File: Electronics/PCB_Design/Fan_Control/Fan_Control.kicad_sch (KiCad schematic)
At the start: 3 parts, among them J2 Conn_01x03, Q1 Q_NMOS_GSD, U1 SeeeduinoXIAO

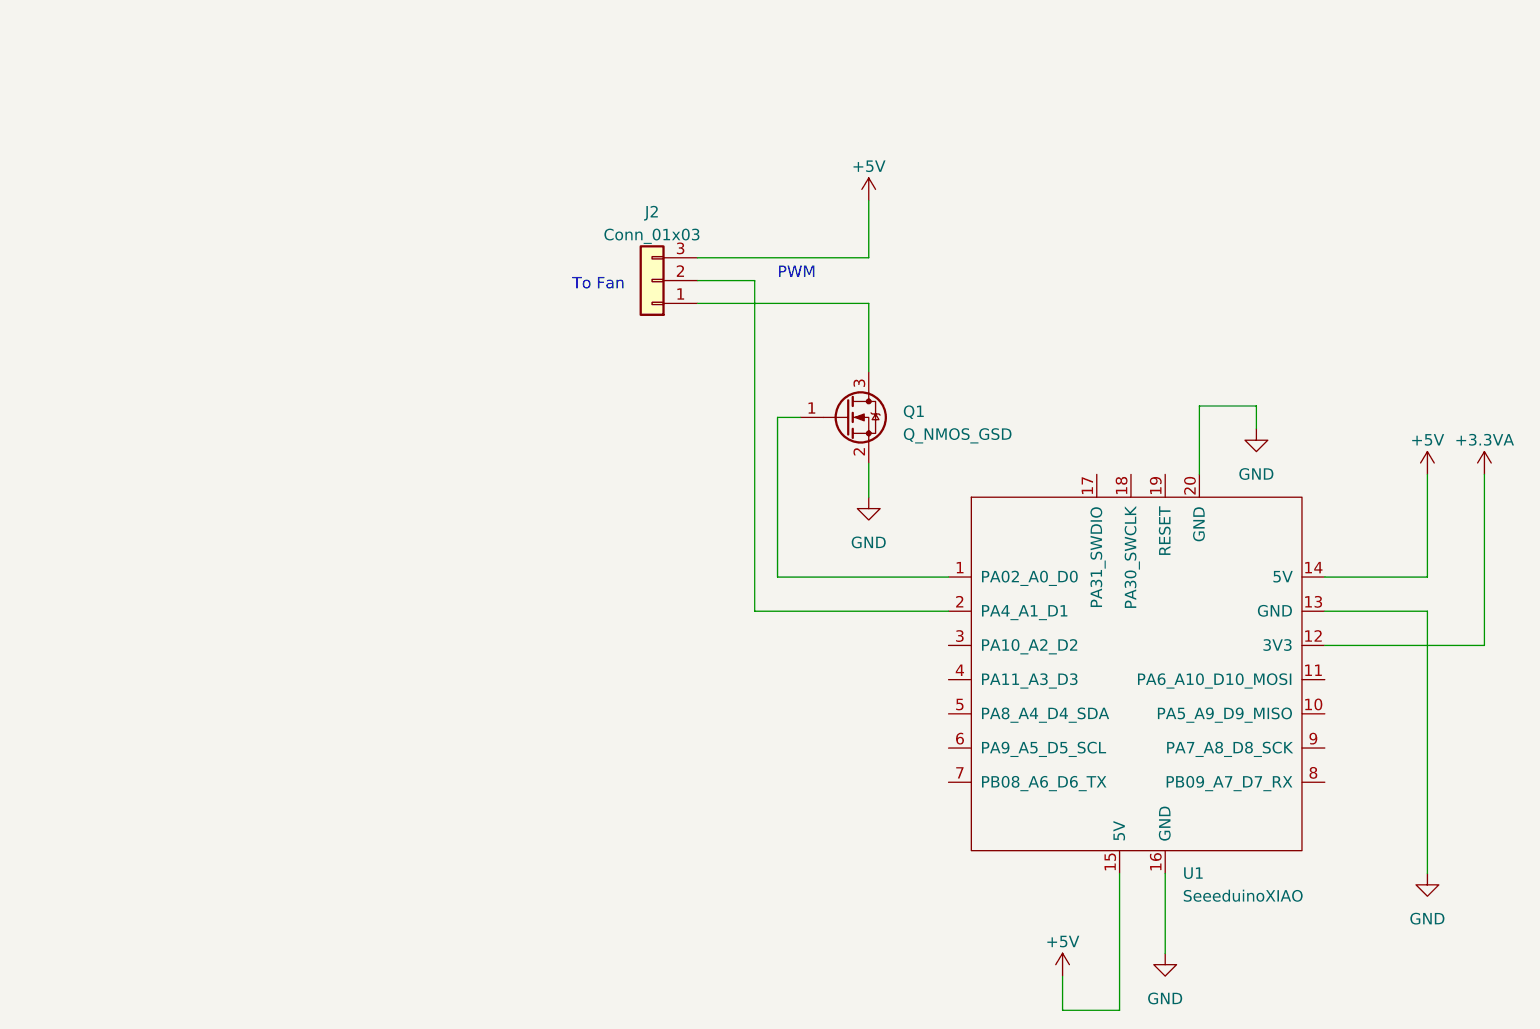
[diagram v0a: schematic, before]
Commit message: Added parts to the schematic and started with circuit design
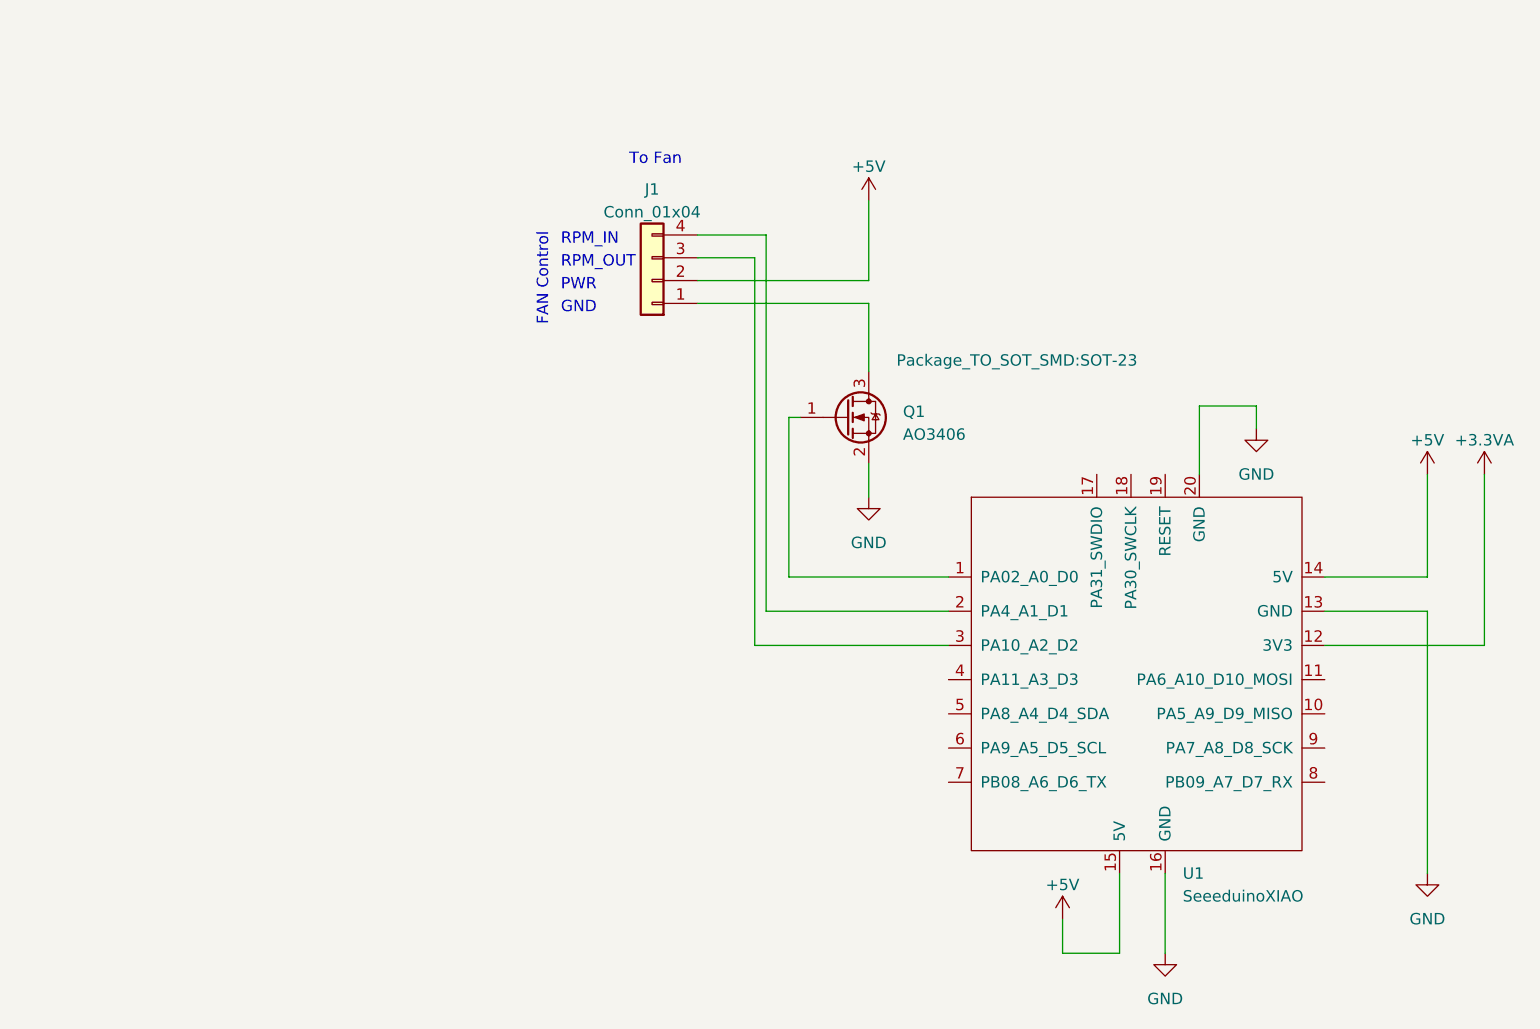
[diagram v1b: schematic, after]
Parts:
- removed J2: Conn_01x03, symbol Connector_Generic:Conn_01x03
- added J1: Conn_01x04, Connector_PinSocket_2.54mm:PinSocket_1x04_P2.54mm_Horizontal, symbol Connector_Generic:Conn_01x04
- Q1: value Q_NMOS_GSD -> AO3406; footprint (none) -> Package_TO_SOT_SMD:SOT-23
- U1: footprint (none) -> Seed studio:Seeeduino XIAO-MOUDLE14P-2.54-21X17.8MM
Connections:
- net +5V: now also J1.2 (Pin_2)
- net at U1.2 (PA4_A1_D1): now also J1.4 (Pin_4)
- net at U1.3 (PA10_A2_D2): now also J1.3 (Pin_3)
- net at Q1.3 (D): now also J1.1 (Pin_1)
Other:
- note added: "FAN Control"
- note added: "GND"
- note added: "PWR"
- note added: "RPM_IN"
- note added: "RPM_OUT"
- note removed: "PWM"
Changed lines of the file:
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@@
 (kicad_sch (version 20230121) (generator eeschema)
   (paper "A4")
-  (wire (pts (xy 104.14 85.09) (xy 104.14 67.31))
+  (wire (pts (xy 123.19 88.9) (xy 102.87 88.9))
+    (stroke (width 0) (type default))
+  )
+  (wire (pts (xy 105.41 85.09) (xy 105.41 67.31))
     (stroke (width 0) (type default))
   )
@@
     (stroke (width 0) (type default))
   )
-  (wire (pts (xy 101.6 88.9) (xy 101.6 52.07))
+  (wire (pts (xy 95.25 46.99) (xy 102.87 46.99))
+    (stroke (width 0) (type default))
+  )
+  (wire (pts (xy 102.87 46.99) (xy 102.87 88.9))
+    (stroke (width 0) (type default))
+  )
+  (wire (pts (xy 101.6 49.53) (xy 101.6 92.71))
     (stroke (width 0) (type default))
   )
@@
     (stroke (width 0) (type default))
   )
-  (wire (pts (xy 123.19 88.9) (xy 101.6 88.9))
-    (stroke (width 0) (type default))
-  )
   (wire (pts (xy 176.53 88.9) (xy 176.53 118.11))
     (stroke (width 0) (type default))
   )
-  (wire (pts (xy 142.24 118.11) (xy 142.24 133.35))
+  (wire (pts (xy 142.24 118.11) (xy 142.24 127))
     (stroke (width 0) (type default))
   )
@@
     (stroke (width 0) (type default))
   )
-  (wire (pts (xy 142.24 133.35) (xy 135.89 133.35))
-    (stroke (width 0) (type default))
-  )
-  (wire (pts (xy 101.6 52.07) (xy 95.25 52.07))
-    (stroke (width 0) (type default))
-  )
-  (wire (pts (xy 104.14 67.31) (xy 106.68 67.31))
-    (stroke (width 0) (type default))
-  )
-  (wire (pts (xy 114.3 43.18) (xy 114.3 49.53))
+  (wire (pts (xy 123.19 92.71) (xy 101.6 92.71))
+    (stroke (width 0) (type default))
+  )
+  (wire (pts (xy 142.24 127) (xy 135.89 127))
+    (stroke (width 0) (type default))
+  )
+  (wire (pts (xy 101.6 49.53) (xy 95.25 49.53))
+    (stroke (width 0) (type default))
+  )
+  (wire (pts (xy 105.41 67.31) (xy 106.68 67.31))
+    (stroke (width 0) (type default))
+  )
+  (wire (pts (xy 114.3 43.18) (xy 114.3 52.07))
     (stroke (width 0) (type default))
   )
@@
     (stroke (width 0) (type default))
   )
-  (wire (pts (xy 95.25 49.53) (xy 114.3 49.53))
+  (wire (pts (xy 95.25 52.07) (xy 114.3 52.07))
     (stroke (width 0) (type default))
   )
@@
     (stroke (width 0) (type default))
   )
-  (wire (pts (xy 135.89 133.35) (xy 135.89 129.54))
-    (stroke (width 0) (type default))
-  )
-  (wire (pts (xy 123.19 85.09) (xy 104.14 85.09))
+  (wire (pts (xy 135.89 127) (xy 135.89 123.19))
+    (stroke (width 0) (type default))
+  )
+  (wire (pts (xy 123.19 85.09) (xy 105.41 85.09))
     (stroke (width 0) (type default))
   )
@@
     (stroke (width 0) (type default))
   )
-  (text "To Fan" (at 81.28 53.34 0)
-    (effects (font (size 1.27 1.27)) (justify left bottom))
-  )
-  (text "PWM" (at 104.14 52.07 0)
-    (effects (font (size 1.27 1.27)) (justify left bottom))
-  )
-  (symbol (lib_id "power:+5V") (at 135.89 129.54 0) (unit 1)
-    (in_bom yes) (on_board yes) (dnp no) (fields_autoplaced)
-    (property "Reference" "#PWR07" (at 135.89 133.35 0)
-      (effects (font (size 1.27 1.27)) hide)
-    )
-    (property "Value" "+5V" (at 135.89 125.73 0)
-      (effects (font (size 1.27 1.27)))
-    )
-    (property "Footprint" "" (at 135.89 129.54 0)
-      (effects (font (size 1.27 1.27)) hide)
-    )
-    (property "Datasheet" "" (at 135.89 129.54 0)
+  (text "RPM_OUT\n" (at 80.01 50.8 0)
+    (effects (font (size 1.27 1.27)) (justify left bottom))
+  )
+  (text "PWR" (at 80.01 53.34 0)
+    (effects (font (size 1.27 1.27)) (justify left bottom))
+  )
+  (text "FAN Control" (at 78.74 57.15 90)
+    (effects (font (size 1.27 1.27)) (justify left bottom))
+  )
+  (text "To Fan" (at 87.63 39.37 0)
+    (effects (font (size 1.27 1.27)) (justify left bottom))
+  )
+  (text "RPM_IN" (at 80.01 48.26 0)
+    (effects (font (size 1.27 1.27)) (justify left bottom))
+  )
+  (text "GND" (at 80.01 55.88 0)
+    (effects (font (size 1.27 1.27)) (justify left bottom))
+  )
+  (symbol (lib_id "power:+5V") (at 135.89 123.19 0) (unit 1)
+    (in_bom yes) (on_board yes) (dnp no) (fields_autoplaced)
+    (property "Reference" "#PWR07" (at 135.89 127 0)
+      (effects (font (size 1.27 1.27)) hide)
+    )
+    (property "Value" "+5V" (at 135.89 119.38 0)
+      (effects (font (size 1.27 1.27)))
+    )
+    (property "Footprint" "" (at 135.89 123.19 0)
+      (effects (font (size 1.27 1.27)) hide)
+    )
+    (property "Datasheet" "" (at 135.89 123.19 0)
       (effects (font (size 1.27 1.27)) hide)
     )
@@
       (effects (font (size 1.27 1.27)) (justify left))
     )
-    (property "Footprint" "" (at 135.89 91.44 0)
+    (property "Footprint" "Seed studio:Seeeduino XIAO-MOUDLE14P-2.54-21X17.8MM" (at 135.89 91.44 0)
       (effects (font (size 1.27 1.27)) hide)
     )
@@
     )
   )
+  (symbol (lib_id "Connector_Generic:Conn_01x04") (at 90.17 52.07 180) (unit 1)
+    (in_bom yes) (on_board yes) (dnp no) (fields_autoplaced)
+    (property "Reference" "J1" (at 90.17 41.91 0)
+      (effects (font (size 1.27 1.27)))
+    )
+    (property "Value" "Conn_01x04" (at 90.17 44.45 0)
+      (effects (font (size 1.27 1.27)))
+    )
+    (property "Footprint" "Connector_PinSocket_2.54mm:PinSocket_1x04_P2.54mm_Horizontal" (at 90.17 52.07 0)
+      (effects (font (size 1.27 1.27)) hide)
+    )
+    (property "Datasheet" "~" (at 90.17 52.07 0)
+      (effects (font (size 1.27 1.27)) hide)
+    )
+    (pin "1")
+    (pin "2")
+    (pin "3")
+    (pin "4")
+    (instances
+      (project "Fan_Control"
+        (path "/dda36686-0e38-4c44-9230-e7c6a57e44b9"
+          (reference "J1") (unit 1)
+        )
+      )
+    )
+  )
   (symbol (lib_id "power:GND") (at 147.32 127 0) (unit 1)
     (in_bom yes) (on_board yes) (dnp no) (fields_autoplaced)
@@
   )
   (symbol (lib_id "Device:Q_NMOS_GSD") (at 111.76 67.31 0) (unit 1)
-    (in_bom yes) (on_board yes) (dnp no) (fields_autoplaced)
+    (in_bom yes) (on_board yes) (dnp no)
     (property "Reference" "Q1" (at 118.11 66.675 0)
       (effects (font (size 1.27 1.27)) (justify left))
     )
-    (property "Value" "Q_NMOS_GSD" (at 118.11 69.215 0)
+    (property "Value" "AO3406" (at 118.11 69.215 0)
       (effects (font (size 1.27 1.27)) (justify left))
     )
-    (property "Footprint" "" (at 116.84 64.77 0)
-      (effects (font (size 1.27 1.27)) hide)
+    (property "Footprint" "Package_TO_SOT_SMD:SOT-23" (at 130.81 60.96 0)
+      (effects (font (size 1.27 1.27)))
     )
     (property "Datasheet" "~" (at 111.76 67.31 0)
@@
         )
       )
-    )
-  )
-  (symbol (lib_id "Connector_Generic:Conn_01x03") (at 90.17 52.07 180) (unit 1)
-    (in_bom yes) (on_board yes) (dnp no) (fields_autoplaced)
-    (property "Reference" "J2" (at 90.17 44.45 0)
-      (effects (font (size 1.27 1.27)))
-    )
-    (property "Value" "Conn_01x03" (at 90.17 46.99 0)
-      (effects (font (size 1.27 1.27)))
-    )
-    (property "Footprint" "" (at 90.17 52.07 0)
-      (effects (font (size 1.27 1.27)) hide)
-    )
-    (property "Datasheet" "~" (at 90.17 52.07 0)
-      (effects (font (size 1.27 1.27)) hide)
-    )
-    (pin "1")
-    (pin "2")
-    (pin "3")
-    (instances
-      (project "Fan_Control"
-        (path "/dda36686-0e38-4c44-9230-e7c6a57e44b9"
-          (reference "J2") (unit 1)
-        )
-      )

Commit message: Added part to hold the power supply
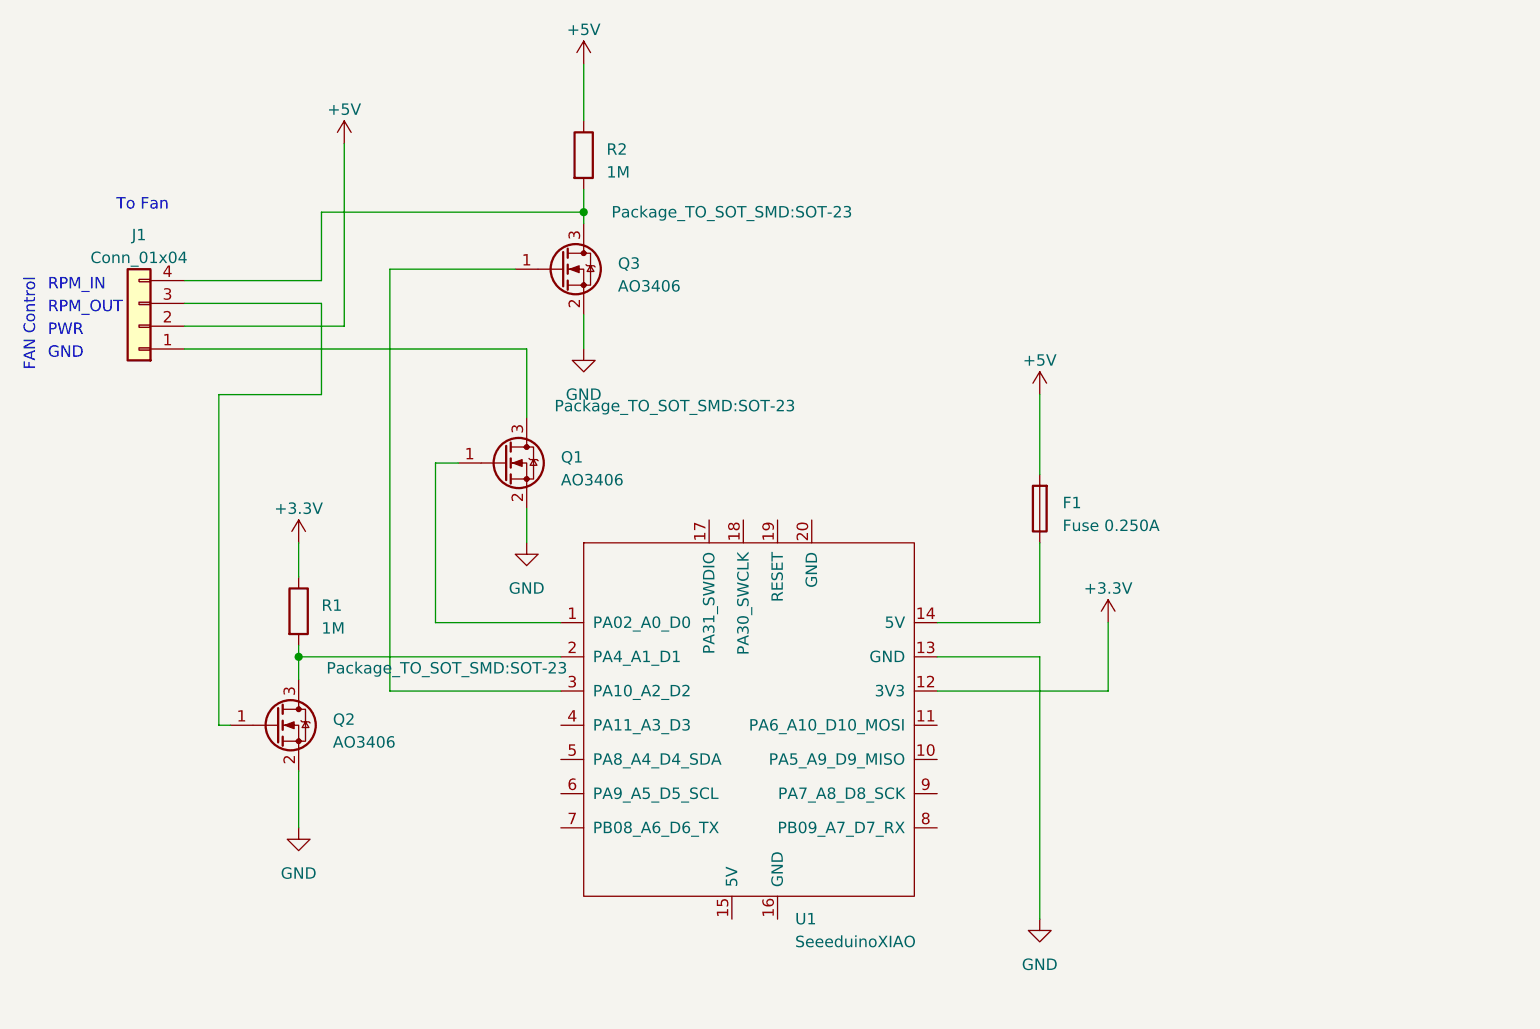
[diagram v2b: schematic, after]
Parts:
- added F1: Fuse 0.250A, Fuse:Fuse_1812_4532Metric, symbol Device:Fuse
- added Q2, Q3: AO3406, Package_TO_SOT_SMD:SOT-23, symbol Device:Q_NMOS_GSD
- added R1, R2: 1M, symbol Device:R
- J1: footprint Connector_PinSocket_2.54mm:PinSocket_1x04_P2.54mm_Horizontal -> TerminalBlock_Phoenix:TerminalBlock_Phoenix_MKDS-1,5-4-5.08_1x04_P5.08mm_Horizontal
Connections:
- net +5V: now also F1.2, R2.1; no longer U1.14 (5V), U1.15 (5V)
- net GND: now also Q2.2 (S), Q3.2 (S); no longer U1.16 (GND), U1.20 (GND)
- net at U1.2 (PA4_A1_D1): now also Q2.3 (D), R1.2; no longer J1.4 (Pin_4)
- net at U1.3 (PA10_A2_D2): now also Q3.1 (G); no longer J1.3 (Pin_3)
- net +3.3VA renamed +3.3V
- net +3.3V: now also R1.1
- new net: F1.1, U1.14 (5V)
- new net: J1.3 (Pin_3), Q2.1 (G)
- new net: J1.4 (Pin_4), Q3.3 (D), R2.2
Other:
- moved on the sheet: J1, Q1, U1
